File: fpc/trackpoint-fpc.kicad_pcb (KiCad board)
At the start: 2 copper layers, 37 x 22.1 mm, 3 parts, among them P1 CONN_8, P2 CONN_5, P3 CONN_8

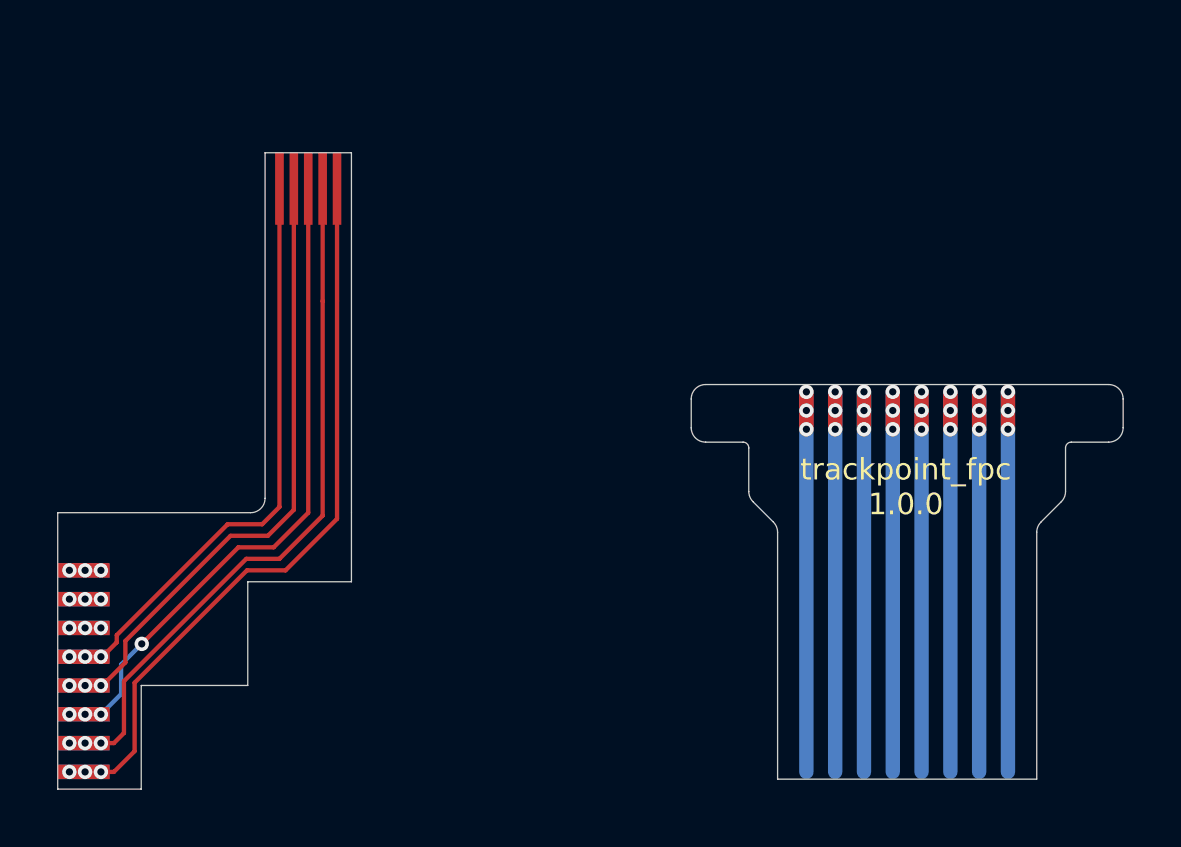
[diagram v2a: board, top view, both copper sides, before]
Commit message: Delete old FPC.
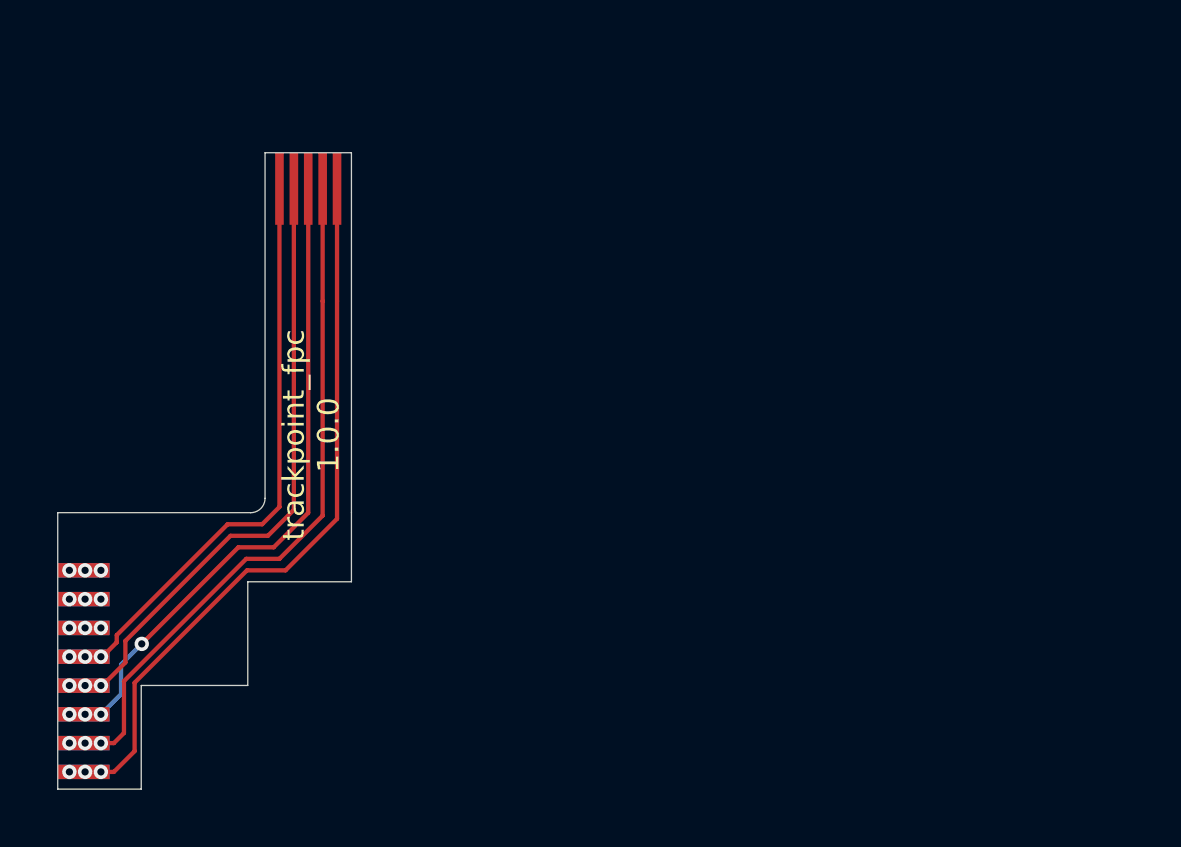
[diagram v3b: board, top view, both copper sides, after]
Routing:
- net (no net): track 116.0 -> 0.00 mm, vias 24 -> 0
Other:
- board size 37 x 22.1 mm -> 10.2 x 22.1 mm
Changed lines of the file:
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@@
   (general
     (thickness 1.6)
-    (drawings 73)
-    (tracks 101)
+    (drawings 30)
+    (tracks 61)
     (zones 0)
     (modules 3)
@@
       (net 1 /VCC))
   )
-  (gr_line (start 223.6 148.952743) (end 223.6 140.377107) (angle 90) (layer Edge.Cuts) (width 0.01))
-  (gr_line (start 223.6 148.952743) (end 214.6 148.952743) (angle 90) (layer Edge.Cuts) (width 0.01))
-  (gr_line (start 223.6 143.952743) (end 214.6 143.952743) (angle 90) (layer Cmts.User) (width 0.01))
-  (gr_line (start 214.6 140.377107) (end 214.6 148.952743) (angle 90) (layer Edge.Cuts) (width 0.01))
   (gr_line (start 199.8 132.2) (end 196.8 132.2) (layer Cmts.User) (width 0.05))
-  (gr_text "trackpoint_fpc\n1.0.0" (at 219.05 138.8) (layer F.SilkS)
+  (gr_text "trackpoint_fpc\n1.0.0" (at 198.4 137 90) (layer F.SilkS)
     (effects (font (size 0.75 0.75) (thickness 0.15)))
   )
@@
   (gr_line (start 199.8 132.2) (end 207.3 132.2) (layer Dwgs.User) (width 0.15))
   (gr_line (start 199.8 127.2) (end 207.3 127.2) (layer Dwgs.User) (width 0.15))
-  (gr_line (start 214.6 146.45) (end 223.6 146.45) (layer B.Mask) (width 5))
-  (gr_line (start 212.05 136.75) (end 226.15 136.75) (layer B.Mask) (width 3))
-  (gr_line (start 212.05 136.25) (end 226.15 136.25) (layer F.Mask) (width 2))
-  (gr_line (start 213.6 137.447257) (end 213.6 138.962893) (angle 90) (layer Edge.Cuts) (width 0.01))
-  (gr_line (start 224.6 137.447257) (end 224.6 138.962893) (angle 90) (layer Edge.Cuts) (width 0.01))
-  (gr_line (start 226.1 135.247257) (end 212.1 135.247257) (angle 90) (layer Edge.Cuts) (width 0.01))
-  (gr_arc (start 214.100005 140.377096) (end 214.6 140.377107) (angle -45.0562246) (layer Edge.Cuts) (width 0.01))
-  (gr_arc (start 214.099995 138.962903) (end 213.6 138.962893) (angle -45.05269373) (layer Edge.Cuts) (width 0.01))
-  (gr_arc (start 224.099995 140.377096) (end 223.746447 140.023553) (angle -44.96338237) (layer Edge.Cuts) (width 0.01))
-  (gr_arc (start 224.100005 138.962903) (end 224.453553 139.316447) (angle -44.96638194) (layer Edge.Cuts) (width 0.01))
-  (gr_arc (start 226.100008 136.747271) (end 226.1 137.247257) (angle -90.00303091) (layer Edge.Cuts) (width 0.01))
-  (gr_arc (start 226.100008 135.747255) (end 226.6 135.747257) (angle -89.99845171) (layer Edge.Cuts) (width 0.01))
-  (gr_arc (start 212.099992 135.747255) (end 212.1 135.247257) (angle -90.00950545) (layer Edge.Cuts) (width 0.01))
-  (gr_arc (start 212.099992 136.747271) (end 211.6 136.747257) (angle -90.01408384) (layer Edge.Cuts) (width 0.01))
-  (gr_line (start 214.453553 140.023553) (end 213.746447 139.316447) (angle 90) (layer Edge.Cuts) (width 0.01))
-  (gr_line (start 224.453553 139.316447) (end 223.746447 140.023553) (angle 90) (layer Edge.Cuts) (width 0.01))
-  (gr_line (start 224.8 137.247257) (end 226.1 137.247257) (angle 90) (layer Edge.Cuts) (width 0.01))
-  (gr_line (start 226.6 136.747257) (end 226.6 135.747257) (angle 90) (layer Edge.Cuts) (width 0.01))
-  (gr_line (start 211.6 135.747257) (end 211.6 136.747257) (angle 90) (layer Edge.Cuts) (width 0.01))
-  (gr_line (start 212.1 137.247257) (end 213.4 137.247257) (angle 90) (layer Edge.Cuts) (width 0.01))
-  (gr_line (start 222.8 137.047257) (end 222.8 135.247257) (angle 90) (layer Cmts.User) (width 0.01))
-  (gr_line (start 222.4 135.247257) (end 222.4 137.047257) (angle 90) (layer Cmts.User) (width 0.01))
-  (gr_line (start 220.4 135.247257) (end 220.4 137.047257) (angle 90) (layer Cmts.User) (width 0.01))
-  (gr_line (start 220.8 137.047257) (end 220.8 135.247257) (angle 90) (layer Cmts.User) (width 0.01))
-  (gr_line (start 218.4 135.247257) (end 218.4 137.047257) (angle 90) (layer Cmts.User) (width 0.01))
-  (gr_line (start 218.8 137.047257) (end 218.8 135.247257) (angle 90) (layer Cmts.User) (width 0.01))
-  (gr_line (start 216.4 135.247257) (end 216.4 137.047257) (angle 90) (layer Cmts.User) (width 0.01))
-  (gr_line (start 216.8 137.047257) (end 216.8 135.247257) (angle 90) (layer Cmts.User) (width 0.01))
-  (gr_line (start 215.4 135.247257) (end 215.4 137.047257) (angle 90) (layer Cmts.User) (width 0.01))
-  (gr_line (start 215.8 137.047257) (end 215.8 135.247257) (angle 90) (layer Cmts.User) (width 0.01))
-  (gr_line (start 217.4 135.247257) (end 217.4 137.047257) (angle 90) (layer Cmts.User) (width 0.01))
-  (gr_line (start 217.8 137.047257) (end 217.8 135.247257) (angle 90) (layer Cmts.User) (width 0.01))
-  (gr_line (start 219.4 135.247257) (end 219.4 137.047257) (angle 90) (layer Cmts.User) (width 0.01))
-  (gr_line (start 219.8 137.047257) (end 219.8 135.247257) (angle 90) (layer Cmts.User) (width 0.01))
-  (gr_line (start 221.4 135.247257) (end 221.4 137.047257) (angle 90) (layer Cmts.User) (width 0.01))
-  (gr_line (start 221.8 137.047257) (end 221.8 135.247257) (angle 90) (layer Cmts.User) (width 0.01))
-  (gr_line (start 211.7 137.047257) (end 226.453553 137.047257) (angle 90) (layer Cmts.User) (width 0.01))
-  (gr_arc (start 213.4 137.447262) (end 213.6 137.447257) (angle -89.98075418) (layer Edge.Cuts) (width 0.01))
-  (gr_arc (start 224.8 137.447262) (end 224.8 137.247257) (angle -90.00839267) (layer Edge.Cuts) (width 0.01))
   (gr_line (start 199.8 127.1975) (end 199.8 139.6975) (angle 90) (layer Edge.Cuts) (width 0.01))
   (gr_line (start 196.8 127.1975) (end 196.8 139.1975) (angle 90) (layer Edge.Cuts) (width 0.01))
@@
   (gr_line (start 199.8 127.1975) (end 196.8 127.1975) (angle 90) (layer Edge.Cuts) (width 0.01))
   (gr_arc (start 196.300006 139.197511) (end 196.3 139.6975) (angle -90.00254177) (layer Edge.Cuts) (width 0.01))
-  (via (at 215.6 135.502257) (size 0.5) (drill 0.25) (layers F.Cu B.Cu) (net 0))
-  (via (at 215.6 136.8) (size 0.5) (drill 0.25) (layers F.Cu B.Cu) (net 0))
-  (via (at 215.6 136.15) (size 0.5) (drill 0.25) (layers F.Cu B.Cu) (net 0))
-  (via (at 216.6 135.502257) (size 0.5) (drill 0.25) (layers F.Cu B.Cu) (net 0))
-  (via (at 217.6 135.5) (size 0.5) (drill 0.25) (layers F.Cu B.Cu) (net 0))
-  (via (at 218.6 135.5) (size 0.5) (drill 0.25) (layers F.Cu B.Cu) (net 0))
-  (via (at 219.6 135.5) (size 0.5) (drill 0.25) (layers F.Cu B.Cu) (net 0))
-  (via (at 220.6 135.5) (size 0.5) (drill 0.25) (layers F.Cu B.Cu) (net 0))
-  (via (at 221.6 135.5) (size 0.5) (drill 0.25) (layers F.Cu B.Cu) (net 0))
-  (via (at 222.6 135.5) (size 0.5) (drill 0.25) (layers F.Cu B.Cu) (net 0))
-  (via (at 216.6 136.8) (size 0.5) (drill 0.25) (layers F.Cu B.Cu) (net 0))
-  (via (at 217.6 136.8) (size 0.5) (drill 0.25) (layers F.Cu B.Cu) (net 0))
-  (via (at 218.6 136.8) (size 0.5) (drill 0.25) (layers F.Cu B.Cu) (net 0))
-  (via (at 219.6 136.8) (size 0.5) (drill 0.25) (layers F.Cu B.Cu) (net 0))
-  (via (at 220.6 136.8) (size 0.5) (drill 0.25) (layers F.Cu B.Cu) (net 0))
-  (via (at 221.6 136.8) (size 0.5) (drill 0.25) (layers F.Cu B.Cu) (net 0))
-  (via (at 222.6 136.8) (size 0.5) (drill 0.25) (layers F.Cu B.Cu) (net 0))
-  (via (at 216.6 136.15) (size 0.5) (drill 0.25) (layers F.Cu B.Cu) (net 0))
-  (via (at 217.6 136.15) (size 0.5) (drill 0.25) (layers F.Cu B.Cu) (net 0))
-  (via (at 218.6 136.15) (size 0.5) (drill 0.25) (layers F.Cu B.Cu) (net 0))
-  (via (at 219.6 136.15) (size 0.5) (drill 0.25) (layers F.Cu B.Cu) (net 0))
-  (via (at 220.6 136.15) (size 0.5) (drill 0.25) (layers F.Cu B.Cu) (net 0))
-  (via (at 221.6 136.15) (size 0.5) (drill 0.25) (layers F.Cu B.Cu) (net 0))
-  (via (at 222.6 136.15) (size 0.5) (drill 0.25) (layers F.Cu B.Cu) (net 0))
-  (segment (start 215.6 135.502257) (end 215.6 136.8) (width 0.5) (layer F.Cu) (net 0))
-  (segment (start 216.6 135.502257) (end 216.6 136.8) (width 0.5) (layer F.Cu) (net 0))
-  (segment (start 217.6 136.8) (end 217.6 135.502267) (width 0.5) (layer F.Cu) (net 0))
-  (segment (start 218.6 136.8) (end 218.6 135.502267) (width 0.5) (layer F.Cu) (net 0))
-  (segment (start 219.6 136.8) (end 219.6 135.502267) (width 0.5) (layer F.Cu) (net 0))
-  (segment (start 220.6 136.8) (end 220.6 135.502267) (width 0.5) (layer F.Cu) (net 0))
-  (segment (start 221.6 136.8) (end 221.6 135.502267) (width 0.5) (layer F.Cu) (net 0))
-  (segment (start 222.6 136.8) (end 222.6 135.502267) (width 0.5) (layer F.Cu) (net 0))
-  (segment (start 218.6 135.5) (end 218.6 148.7) (width 0.5) (layer B.Cu) (net 0))
-  (segment (start 222.6 135.5) (end 222.6 148.7) (width 0.5) (layer B.Cu) (net 0))
-  (segment (start 216.6 135.5) (end 216.6 148.7) (width 0.5) (layer B.Cu) (net 0))
-  (segment (start 221.6 135.5) (end 221.6 148.7) (width 0.5) (layer B.Cu) (net 0))
-  (segment (start 217.6 135.5) (end 217.6 148.7) (width 0.5) (layer B.Cu) (net 0))
-  (segment (start 220.6 135.5) (end 220.6 148.7) (width 0.5) (layer B.Cu) (net 0))
-  (segment (start 219.6 135.5) (end 219.6 148.7) (width 0.5) (layer B.Cu) (net 0))
-  (segment (start 215.6 135.5) (end 215.6 148.7) (width 0.5) (layer B.Cu) (net 0))
   (segment (start 199.3 139.912139) (end 199.3 132.35) (width 0.15) (layer F.Cu) (net 1))
   (segment (start 197.512139 141.7) (end 199.3 139.912139) (width 0.15) (layer F.Cu) (net 1))

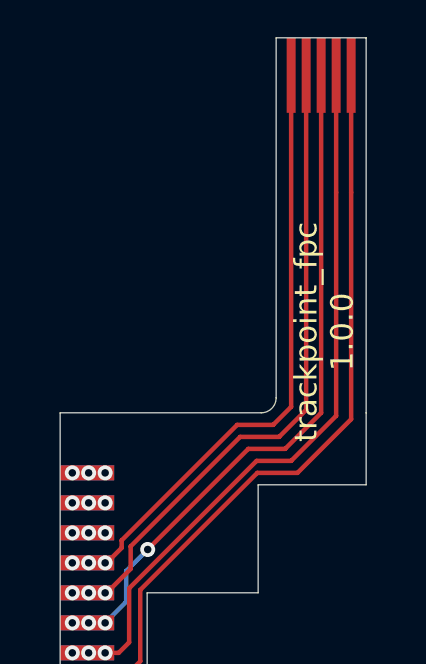
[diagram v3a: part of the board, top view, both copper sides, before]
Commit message: Bump FPC version to 2.0.0
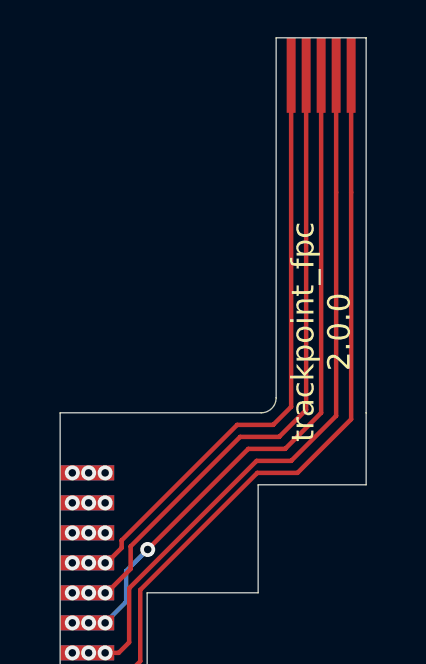
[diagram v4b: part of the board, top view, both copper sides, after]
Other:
- board text added: "trackpoint_fpc 2.0.0"
- board text removed: "trackpoint_fpc 1.0.0"
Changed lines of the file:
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@@
   (title_block
     (title "UHK Trackpoint FPC")
-    (rev 1.0.0)
+    (rev 2.0.0)
     (company "Ultimate Gadget Laboratories Kft.")
   )
@@
   )
   (gr_line (start 199.8 132.2) (end 196.8 132.2) (layer Cmts.User) (width 0.05))
-  (gr_text "trackpoint_fpc\n1.0.0" (at 198.4 137 90) (layer F.SilkS)
+  (gr_text "trackpoint_fpc\n2.0.0" (at 198.3 137 90) (layer F.SilkS)
     (effects (font (size 0.75 0.75) (thickness 0.15)))
   )

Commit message: Change stiffener side.
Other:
- board text added: "Stiffener BOTTOM"
- board text removed: "Stiffener TOP"
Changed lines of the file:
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@@
   )
   (gr_line (start 199.8 132.2) (end 196.8 132.2) (layer Cmts.User) (width 0.05))
-  (gr_text "trackpoint_fpc\n2.0.0" (at 198.3 137 90) (layer F.SilkS)
+  (gr_text "trackpoint_fpc\n2.0.0" (at 198.3 135.8 90) (layer F.SilkS)
     (effects (font (size 0.75 0.75) (thickness 0.15)))
   )
-  (gr_text "Stiffener TOP" (at 205.35 129.7) (layer Dwgs.User)
+  (gr_text "Stiffener BOTTOM" (at 206.6 129.7) (layer Dwgs.User)
     (effects (font (size 1 1) (thickness 0.15)))
   )
